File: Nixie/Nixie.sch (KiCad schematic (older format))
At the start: 28 parts

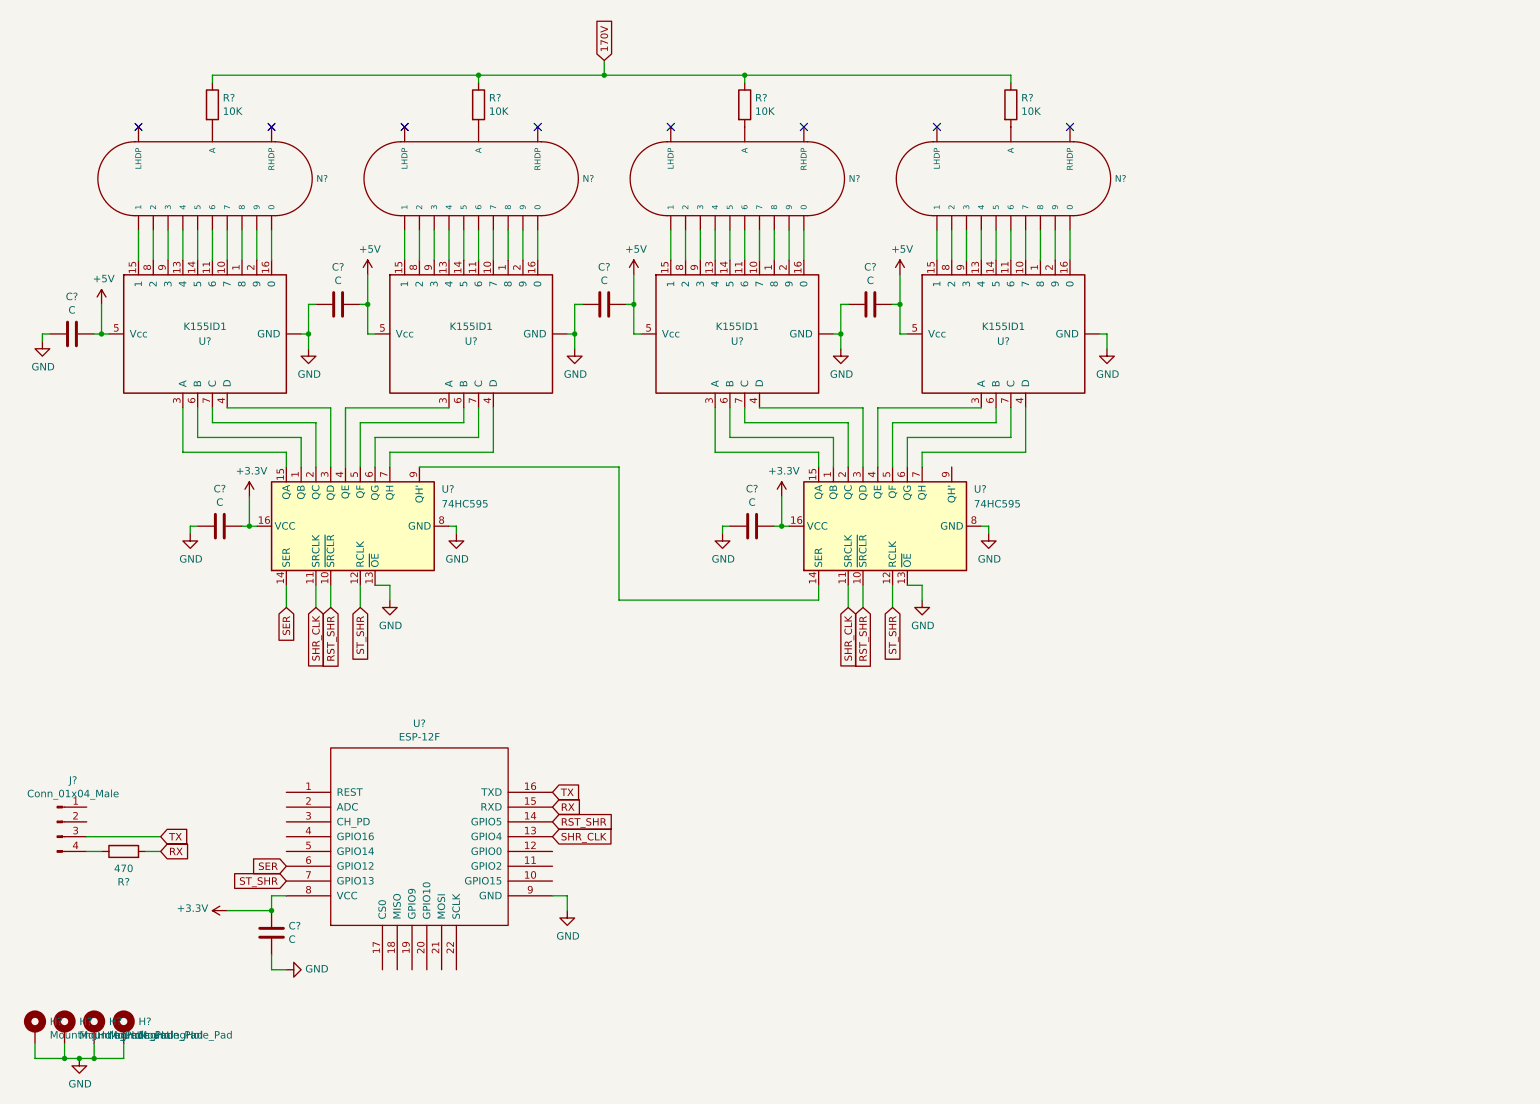
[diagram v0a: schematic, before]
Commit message: 5V -> 3.3V hinzugefügt
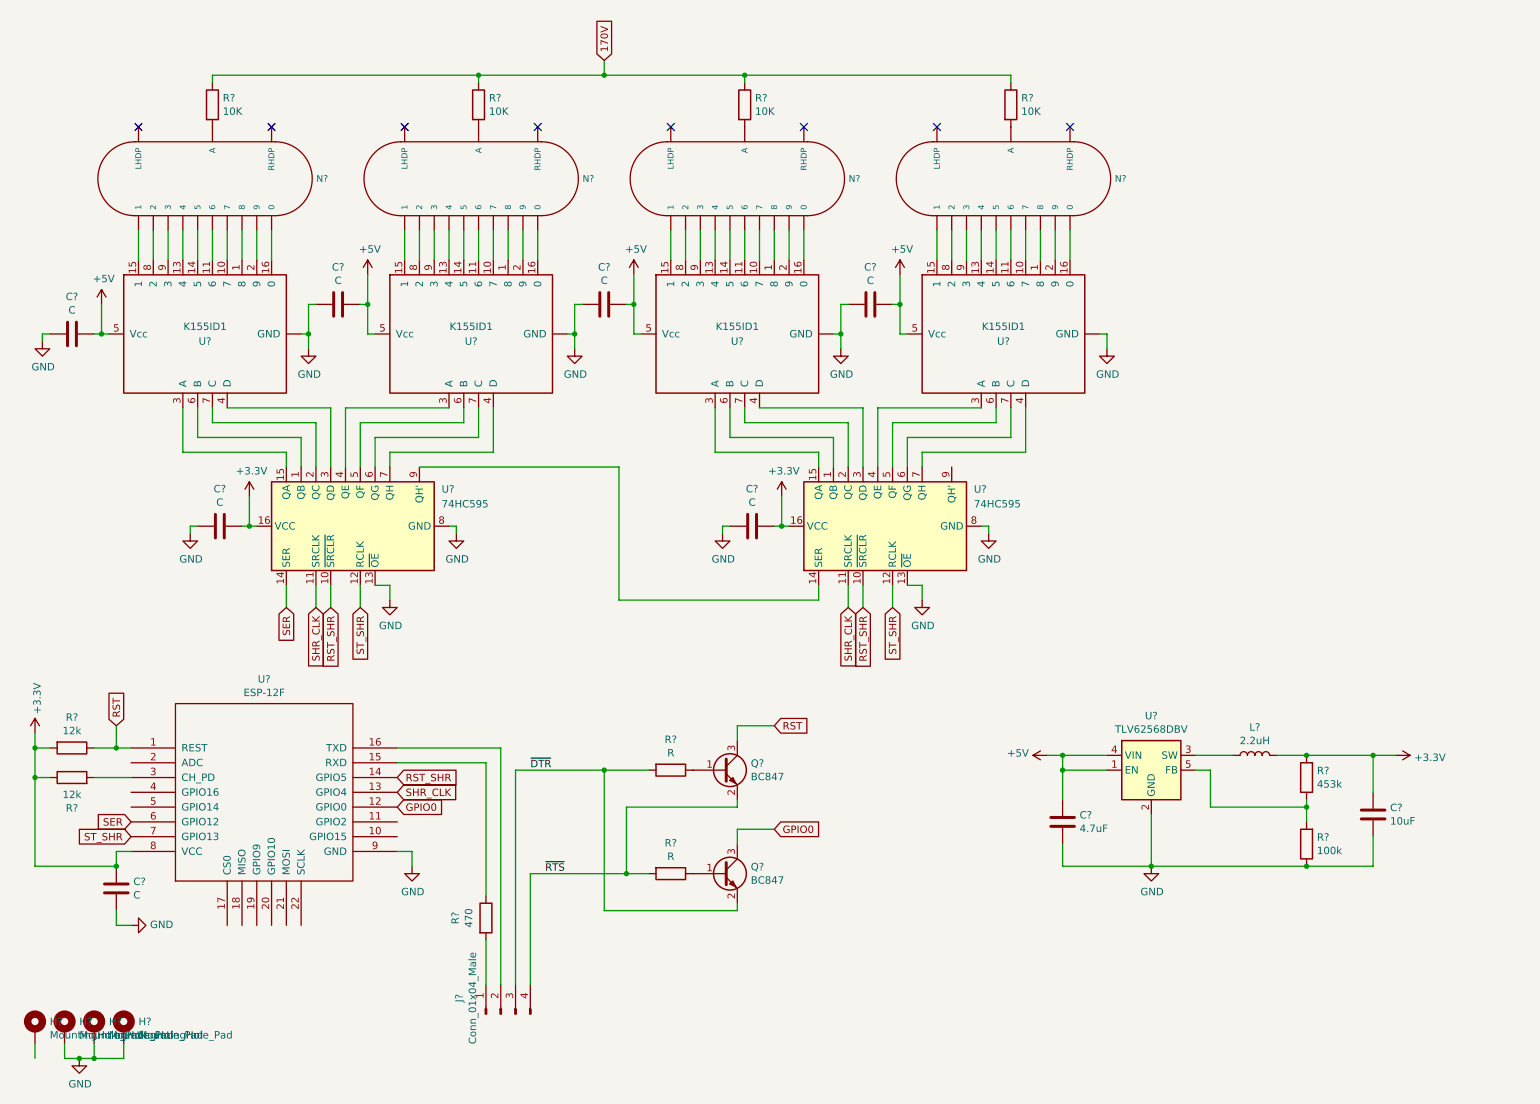
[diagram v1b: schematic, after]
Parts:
- added C?: 10uF, symbol Device:C
- added C?: 4.7uF, symbol Device:C
- added L?: 2.2uH, symbol Device:L
- added Q? (x2): BC847, Package_TO_SOT_SMD:SOT-23, symbol Transistor_BJT:BC847
- added R?: 453k, symbol Device:R
- added R?: 100k, symbol Device:R
- added R? (x2): R, symbol Device:R
- added R? (x2): 12k, symbol Device:R
- added U?: TLV62568DBV, Package_TO_SOT_SMD:SOT-23-5, symbol Regulator_Switching:TLV62568DBV
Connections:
- net +3V3: now also C?.1, L?.2, R?.1, R?.2, R?.2
- net +5V: now also C?.1, U?.1 (EN), U?.4 (VIN)
- net GND: now also C?.2, C?.2, R?.1, U?.2 (GND); no longer H?.1
- net RST: now reaches U?.1 (REST)
- net RST: now also Q?.3 (C), R?.1
- net GPIO0: now reaches U?.12 (GPIO0)
- net GPIO0: now also Q?.3 (C)
- net at U?.3 (CH_PD): now also R?.2
- net at J?.1 (Pin_1): now also R?.2
- net at J?.2 (Pin_2): now also U?.16 (TXD)
- net at R?.1: now also U?.15 (RXD); no longer J?.4 (Pin_4)
- removed net RX: R?.2, U?.15 (RXD)
- net TX renamed ~DTR
- net ~DTR: now also Q?.2 (E), R?.2; no longer U?.16 (TXD)
- new net: Q?.1 (B), R?.1 (x2)
- new net: L?.1, U?.3 (SW)
- new net: R?.1, R?.2, U?.5 (FB)
- new net ~RTS: J?.4 (Pin_4), Q?.2 (E), R?.2
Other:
- moved on the sheet: C?, J?, R?, U?

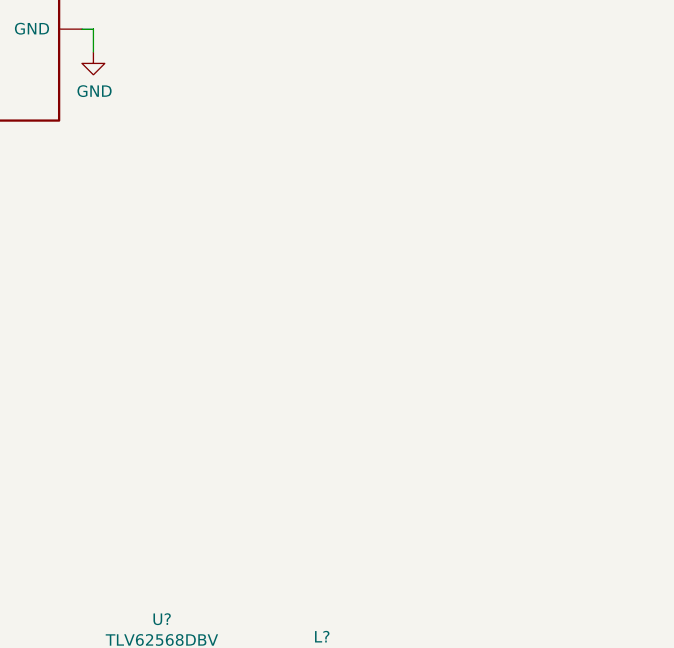
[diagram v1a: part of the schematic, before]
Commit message: USB Header hinzugefügt
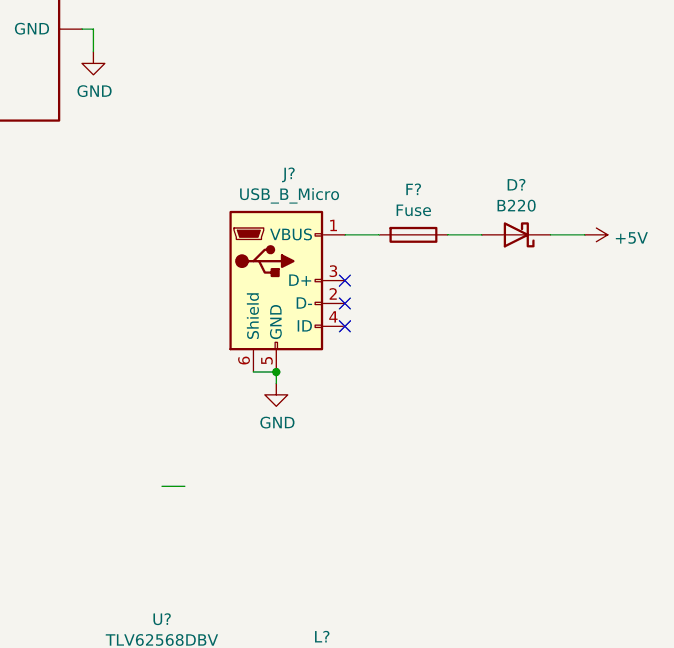
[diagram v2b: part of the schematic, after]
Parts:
- added D?: B220, Diode_SMD:D_SMB, symbol Diode:B220
- added F?: Fuse, symbol Device:Fuse
- added J?: USB_B_Micro, symbol Connector:USB_B_Micro
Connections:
- net +5V: now also D?.1 (K)
- net GND: now also J?.5 (GND), J?.6 (Shield)
- new net: F?.2, J?.1 (VBUS)
- new net: D?.2 (A), F?.1
- no-connect marks 8 -> 11
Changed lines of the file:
@@
 	7600 5500 7500 5500
 Connection ~ 7600 5500
+$Comp
+L Connector:USB_B_Micro J?
+U 1 1 6074AE4C
+P 8700 3750
+F 0 "J?" H 8757 4217 50  0000 C CNN
+F 1 "USB_B_Micro" H 8757 4126 50  0000 C CNN
+F 2 "" H 8850 3700 50  0001 C CNN
+F 3 "~" H 8850 3700 50  0001 C CNN
+	1    8700 3750
+	1    0    0    -1
+$EndComp
+Wire Wire Line
+	8200 4650 8300 4650
+Wire Wire Line
+	8600 4150 8700 4150
+Connection ~ 8700 4150
+$Comp
+L power:GND #PWR?
+U 1 1 607A30F8
+P 8700 4200
+F 0 "#PWR?" H 8700 3950 50  0001 C CNN
+F 1 "GND" H 8705 4027 50  0000 C CNN
+F 2 "" H 8700 4200 50  0001 C CNN
+F 3 "" H 8700 4200 50  0001 C CNN
+	1    8700 4200
+	1    0    0    -1
+$EndComp
+Wire Wire Line
+	8700 4200 8700 4150
+$Comp
+L Device:Fuse F?
+U 1 1 607B253F
+P 9300 3550
+F 0 "F?" V 9103 3550 50  0000 C CNN
+F 1 "Fuse" V 9194 3550 50  0000 C CNN
+F 2 "" V 9230 3550 50  0001 C CNN
+F 3 "~" H 9300 3550 50  0001 C CNN
+	1    9300 3550
+	0    1    1    0
+$EndComp
+$Comp
+L Diode:B220 D?
+U 1 1 607F8990
+P 9750 3550
+F 0 "D?" H 9750 3333 50  0000 C CNN
+F 1 "B220" H 9750 3424 50  0000 C CNN
+F 2 "Diode_SMD:D_SMB" H 9750 3375 50  0001 C CNN
+F 3 "http://www.jameco.com/Jameco/Products/ProdDS/1538777.pdf" H 9750 3550 50  0001 C CNN
+	1    9750 3550
+	-1   0    0    1
+$EndComp
+Wire Wire Line
+	9600 3550 9450 3550
+Wire Wire Line
+	9150 3550 9000 3550
+$Comp
+L power:+5V #PWR?
+U 1 1 608247EB
+P 10050 3550
+F 0 "#PWR?" H 10050 3400 50  0001 C CNN
+F 1 "+5V" V 10065 3678 50  0000 L CNN
+F 2 "" H 10050 3550 50  0001 C CNN
+F 3 "" H 10050 3550 50  0001 C CNN
+	1    10050 3550
+	0    1    1    0
+$EndComp
+Wire Wire Line
+	10050 3550 9900 3550
+NoConn ~ 9000 3950
+NoConn ~ 9000 3850
+NoConn ~ 9000 3750
 $EndSCHEMATC

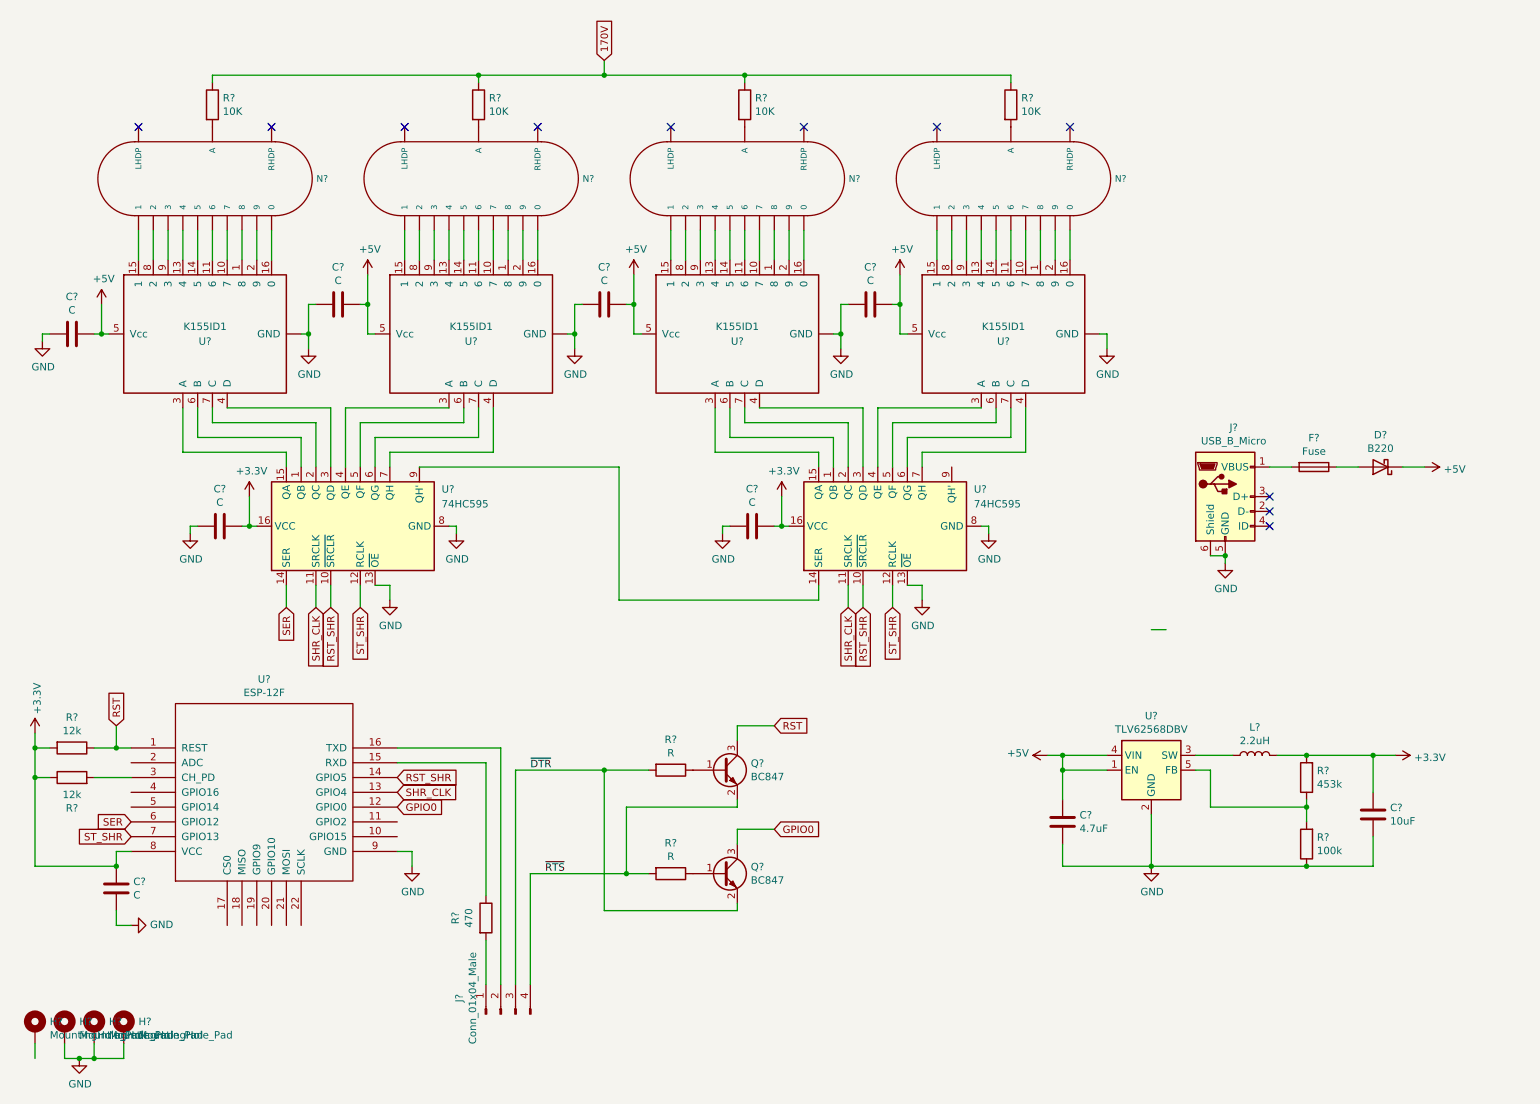
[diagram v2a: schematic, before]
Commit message: 5v to 170v Step Up hinzugefügt
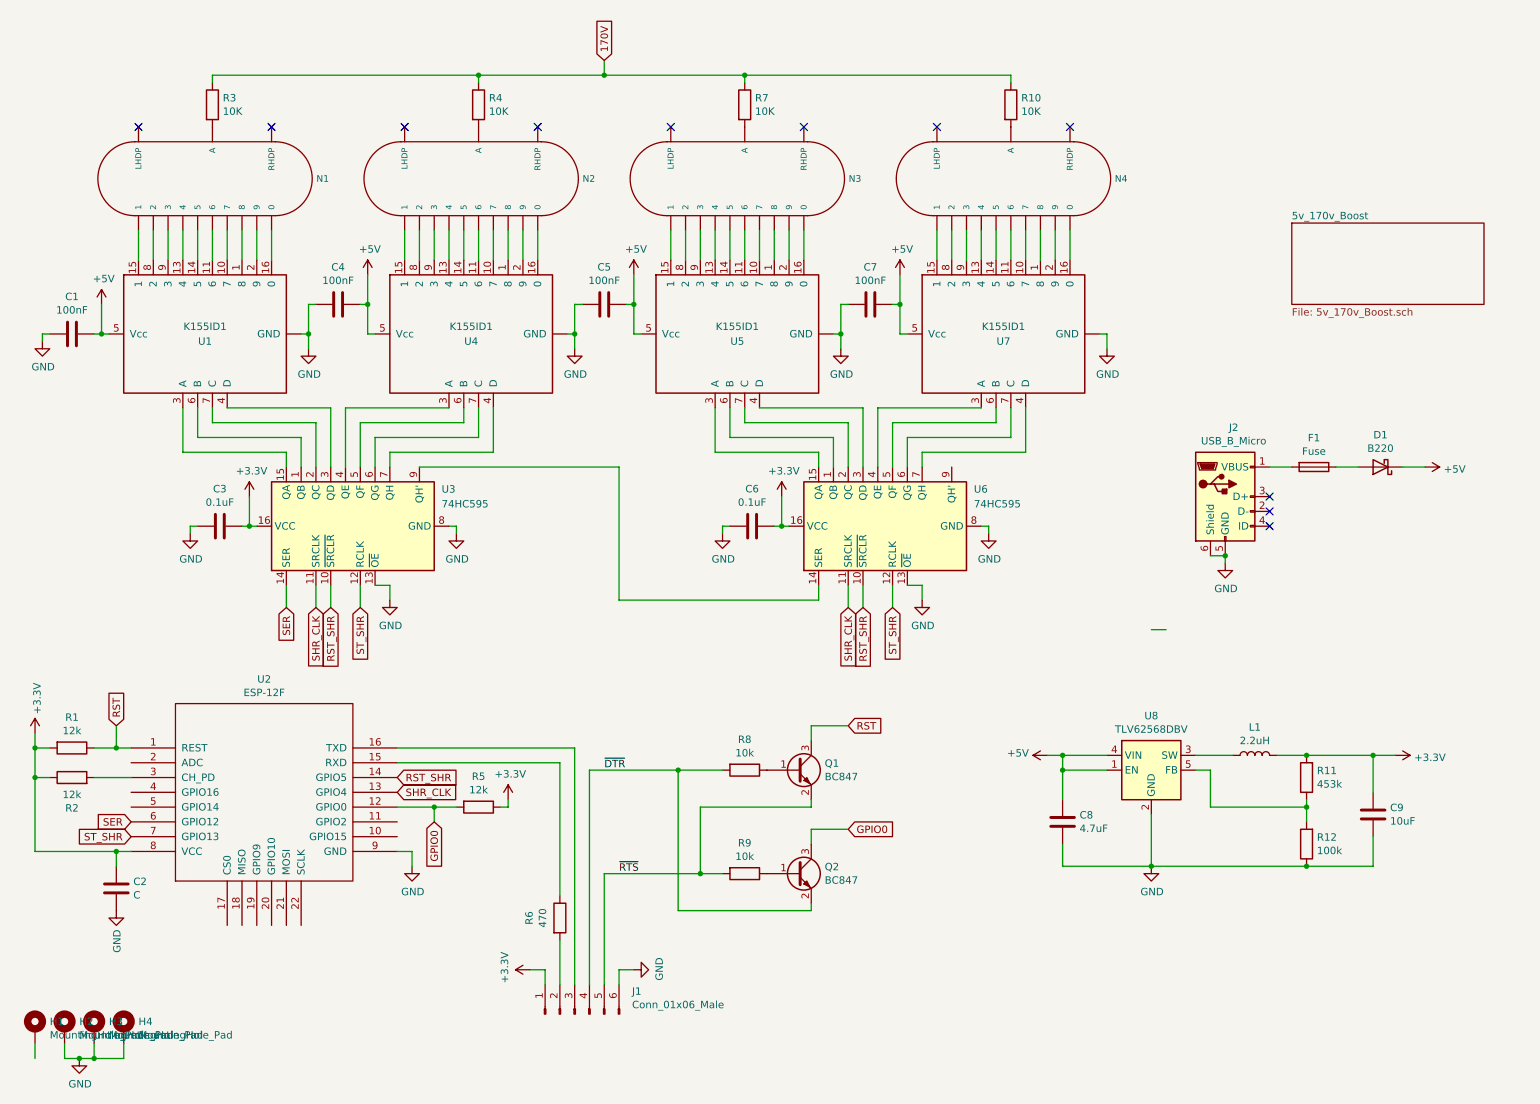
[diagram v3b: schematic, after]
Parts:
- removed J?: Conn_01x04_Male, symbol Connector:Conn_01x04_Male
- added J1: Conn_01x06_Male, symbol Connector:Conn_01x06_Male
- added R5: 12k, symbol Device:R
- C1, C4, C5, C7: renamed from C?; value C -> 100nF
- C3, C6: renamed from C?; value C -> 0.1uF
- R8, R9: renamed from R?; value R -> 10k
- gave numbers to parts that had none: 34
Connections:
- net +3V3: now also J1.1 (Pin_1), R5.1
- net GND: now also J1.6 (Pin_6)
- net GPIO0: now also R5.2
- net ~DTR: now also J1.4 (Pin_4)
- net ~RTS: now also J1.5 (Pin_5)
- net at U2.16 (TXD): now also J1.3 (Pin_3)
- net at R6.2: now also J1.2 (Pin_2)
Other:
- moved on the sheet: Q1, Q2, R6, R8, R9

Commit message: Werte angeglichen
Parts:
- C1, C4, C5, C7: value 100nF -> 0.1uF
- C2: value C -> 0.1uF
- R10, R3, R4, R7: value 10K -> 10k
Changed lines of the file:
@@
 P 2700 2450
 F 0 "C4" V 2448 2450 50  0000 C CNN
-F 1 "100nF" V 2539 2450 50  0000 C CNN
+F 1 "0.1uF" V 2539 2450 50  0000 C CNN
 F 2 "" H 2738 2300 50  0001 C CNN
 F 3 "~" H 2700 2450 50  0001 C CNN
@@
 P 4500 2450
 F 0 "C5" V 4248 2450 50  0000 C CNN
-F 1 "100nF" V 4339 2450 50  0000 C CNN
+F 1 "0.1uF" V 4339 2450 50  0000 C CNN
 F 2 "" H 4538 2300 50  0001 C CNN
 F 3 "~" H 4500 2450 50  0001 C CNN
@@
 P 6300 2450
 F 0 "C7" V 6048 2450 50  0000 C CNN
-F 1 "100nF" V 6139 2450 50  0000 C CNN
+F 1 "0.1uF" V 6139 2450 50  0000 C CNN
 F 2 "" H 6338 2300 50  0001 C CNN
 F 3 "~" H 6300 2450 50  0001 C CNN
@@
 P 900 2650
 F 0 "C1" V 648 2650 50  0000 C CNN
-F 1 "100nF" V 739 2650 50  0000 C CNN
+F 1 "0.1uF" V 739 2650 50  0000 C CNN
 F 2 "" H 938 2500 50  0001 C CNN
 F 3 "~" H 900 2650 50  0001 C CNN
@@
 P 1850 1100
 F 0 "R3" H 1920 1146 50  0000 L CNN
-F 1 "10K" H 1920 1055 50  0000 L CNN
+F 1 "10k" H 1920 1055 50  0000 L CNN
 F 2 "" V 1780 1100 50  0001 C CNN
 F 3 "~" H 1850 1100 50  0001 C CNN
@@
 P 3650 1100
 F 0 "R4" H 3720 1146 50  0000 L CNN
-F 1 "10K" H 3720 1055 50  0000 L CNN
+F 1 "10k" H 3720 1055 50  0000 L CNN
 F 2 "" V 3580 1100 50  0001 C CNN
 F 3 "~" H 3650 1100 50  0001 C CNN
@@
 P 5450 1100
 F 0 "R7" H 5520 1146 50  0000 L CNN
-F 1 "10K" H 5520 1055 50  0000 L CNN
+F 1 "10k" H 5520 1055 50  0000 L CNN
 F 2 "" V 5380 1100 50  0001 C CNN
 F 3 "~" H 5450 1100 50  0001 C CNN
@@
 P 7250 1100
 F 0 "R10" H 7320 1146 50  0000 L CNN
-F 1 "10K" H 7320 1055 50  0000 L CNN
+F 1 "10k" H 7320 1055 50  0000 L CNN
 F 2 "" V 7180 1100 50  0001 C CNN
 F 3 "~" H 7250 1100 50  0001 C CNN
@@
 P 1200 6400
 F 0 "C2" H 1315 6446 50  0000 L CNN
-F 1 "C" H 1315 6355 50  0000 L CNN
+F 1 "0.1uF" H 1315 6355 50  0000 L CNN
 F 2 "" H 1238 6250 50  0001 C CNN
 F 3 "~" H 1200 6400 50  0001 C CNN

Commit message: Kleinere Anpassungen
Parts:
- removed C8: 4.7uF, symbol Device:C
- removed C9: 10uF, symbol Device:C
- removed D1: B220, Diode_SMD:D_SMB, symbol Diode:B220
- removed F1: Fuse, symbol Device:Fuse
- removed J2: USB_B_Micro, symbol Connector:USB_B_Micro
- removed L1: 2.2uH, symbol Device:L
- removed R1, R2, R5: 12k, symbol Device:R
- removed R11: 453k, symbol Device:R
- removed R12: 100k, symbol Device:R
- removed U8: TLV62568DBV, Package_TO_SOT_SMD:SOT-23-5, symbol Regulator_Switching:TLV62568DBV
- added C? (x2): 330uF, symbol Device:C
- added D?: 1N5819, Diode_THT:D_DO-41_SOD81_P10.16mm_Horizontal, symbol Diode:1N5819
- added J?: USB_B_Micro, symbol Connector:USB_B_Micro
- added L?: 330uH, symbol Device:L
- added U?: LM2575-3.3BT, Package_TO_SOT_THT:TO-220-5_Vertical, symbol Regulator_Switching:LM2575-3.3BT
- R8, R9: value 10k -> 12k
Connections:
- net +3V3: now also U2.3 (CH_PD), C?.1, L?.2, U?.4 (FB)
- net +5V: now also C?.1, J?.1 (VBUS), U?.1 (VIN)
- net GND: now also C?.2, C?.2, D?.2 (A), J?.5 (GND), U?.3 (GND), U?.5 (~ON~/OFF)
- net ~DTR renamed DTR
- net ~RTS renamed RTS
- new net: D?.1 (K), L?.1, U?.2 (OUT)
- no-connect marks 11 -> 8
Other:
- note added: "5V -> 3.3V\n"
- note added: "Autoflash"
